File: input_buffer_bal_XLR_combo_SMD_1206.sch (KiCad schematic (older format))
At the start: 31 parts, among them J1 CH1, J2 CH2, J3 POWER, J4 CH1_OUT, J5 CH2_OUT, U1 LM4562, U2 LM4562

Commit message: Changed footprint for TVS diodes to DFN1006
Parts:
- D1, D2, D3, D4: footprint Diode_SMD:D_SOD-123F -> local_footprint_lib:D_DFN1006
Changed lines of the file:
@@
 F 0 "D1" V 3454 1830 50  0000 L CNN
 F 1 "SMF6.0CA" V 3545 1830 50  0000 L CNN
-F 2 "Diode_SMD:D_SOD-123F" H 3500 1750 50  0001 C CNN
+F 2 "local_footprint_lib:D_DFN1006" H 3500 1750 50  0001 C CNN
 F 3 "~" H 3500 1750 50  0001 C CNN
 	1    3500 1750
@@
 F 0 "D2" V 3454 2330 50  0000 L CNN
 F 1 "SMF6.0CA" V 3545 2330 50  0000 L CNN
-F 2 "Diode_SMD:D_SOD-123F" H 3500 2250 50  0001 C CNN
+F 2 "local_footprint_lib:D_DFN1006" H 3500 2250 50  0001 C CNN
 F 3 "~" H 3500 2250 50  0001 C CNN
 	1    3500 2250
@@
 F 0 "D3" V 3454 3830 50  0000 L CNN
 F 1 "SMF6.0CA" V 3545 3830 50  0000 L CNN
-F 2 "Diode_SMD:D_SOD-123F" H 3500 3750 50  0001 C CNN
+F 2 "local_footprint_lib:D_DFN1006" H 3500 3750 50  0001 C CNN
 F 3 "~" H 3500 3750 50  0001 C CNN
 	1    3500 3750
@@
 F 0 "D4" V 3454 4330 50  0000 L CNN
 F 1 "SMF6.0CA" V 3545 4330 50  0000 L CNN
-F 2 "Diode_SMD:D_SOD-123F" H 3500 4250 50  0001 C CNN
+F 2 "local_footprint_lib:D_DFN1006" H 3500 4250 50  0001 C CNN
 F 3 "~" H 3500 4250 50  0001 C CNN
 	1    3500 4250

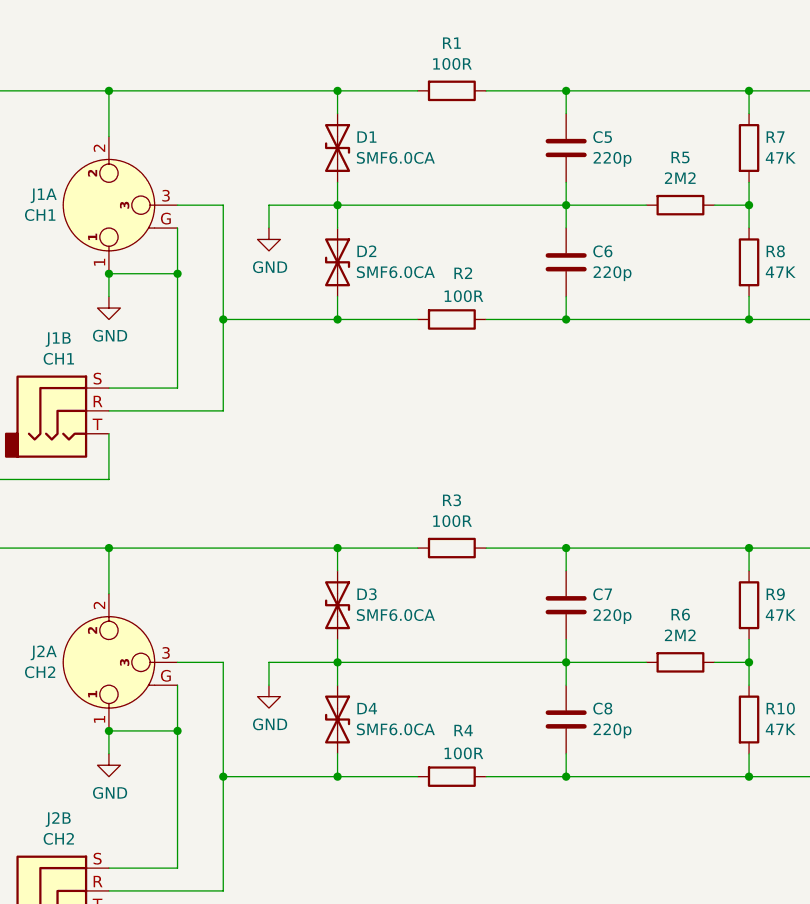
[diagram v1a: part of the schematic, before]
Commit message: updated TVS diode
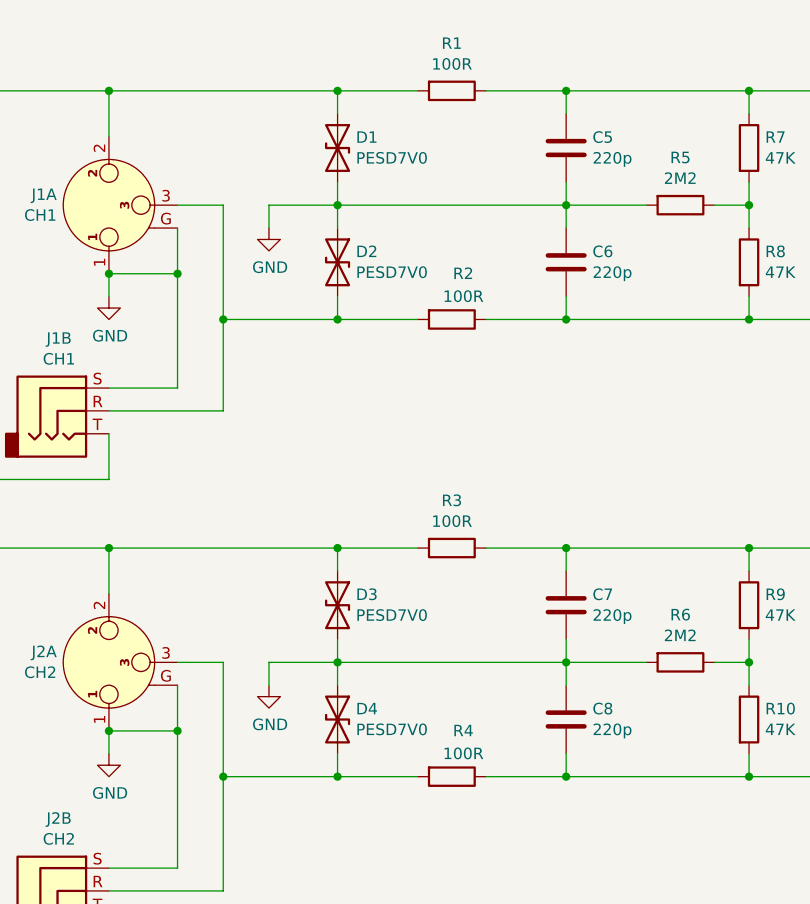
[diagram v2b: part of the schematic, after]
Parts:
- D1, D2, D3, D4: value SMF6.0CA -> PESD7V0
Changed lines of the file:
@@
 P 3500 1750
 F 0 "D1" V 3454 1830 50  0000 L CNN
-F 1 "SMF6.0CA" V 3545 1830 50  0000 L CNN
+F 1 "PESD7V0" V 3545 1830 50  0000 L CNN
 F 2 "local_footprint_lib:D_DFN1006" H 3500 1750 50  0001 C CNN
 F 3 "~" H 3500 1750 50  0001 C CNN
@@
 P 3500 2250
 F 0 "D2" V 3454 2330 50  0000 L CNN
-F 1 "SMF6.0CA" V 3545 2330 50  0000 L CNN
+F 1 "PESD7V0" V 3545 2330 50  0000 L CNN
 F 2 "local_footprint_lib:D_DFN1006" H 3500 2250 50  0001 C CNN
 F 3 "~" H 3500 2250 50  0001 C CNN
@@
 P 3500 3750
 F 0 "D3" V 3454 3830 50  0000 L CNN
-F 1 "SMF6.0CA" V 3545 3830 50  0000 L CNN
+F 1 "PESD7V0" V 3545 3830 50  0000 L CNN
 F 2 "local_footprint_lib:D_DFN1006" H 3500 3750 50  0001 C CNN
 F 3 "~" H 3500 3750 50  0001 C CNN
@@
 P 3500 4250
 F 0 "D4" V 3454 4330 50  0000 L CNN
-F 1 "SMF6.0CA" V 3545 4330 50  0000 L CNN
+F 1 "PESD7V0" V 3545 4330 50  0000 L CNN
 F 2 "local_footprint_lib:D_DFN1006" H 3500 4250 50  0001 C CNN
 F 3 "~" H 3500 4250 50  0001 C CNN
